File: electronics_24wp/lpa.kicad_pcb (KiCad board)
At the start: 2 copper layers, 143 x 74 mm, 89 parts, among them IC1 ATMEGA328-A, P1 CONN_2, P2 CONN_3X2, U1 SD_CARD, U2 LD1117S33, U3 TLC5941, U4 TLC5941, U5 TLC5941, Y1 RESONATEUR

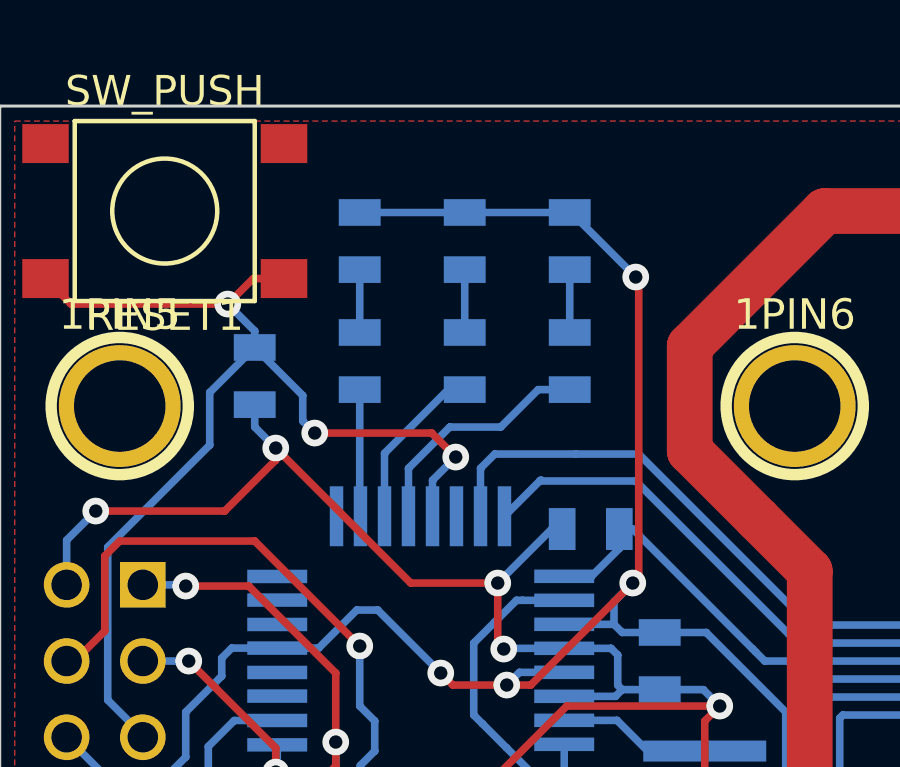
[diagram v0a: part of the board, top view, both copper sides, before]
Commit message: Changed the orientation of the leds in the electronic board.
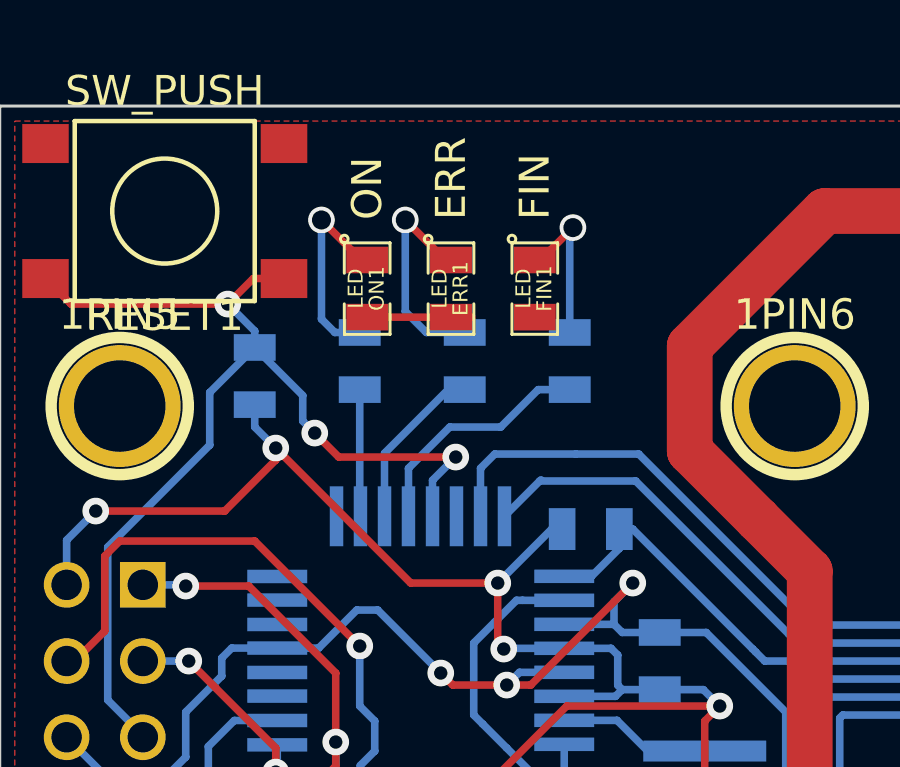
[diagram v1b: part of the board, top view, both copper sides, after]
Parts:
- ERR1, FIN1, ON1: moved to F.Cu
- moved FIN1 1.97 mm to (84.8, 100.6), turned to 270 degrees
- moved ERR1 1.65 mm to (82.0, 100.6), turned to 270 degrees
- moved ON1 1.60 mm to (79.2, 100.6), turned to 270 degrees
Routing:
- net GND: track 152.8 -> 136.1 mm, vias 7 -> 6
- net N-000005: track 2.09 -> 7.40 mm, vias 0 -> 1
- net N-000004: track 2.09 -> 6.84 mm, vias 0 -> 1
- net N-000006: track 2.09 -> 5.42 mm, vias 0 -> 1

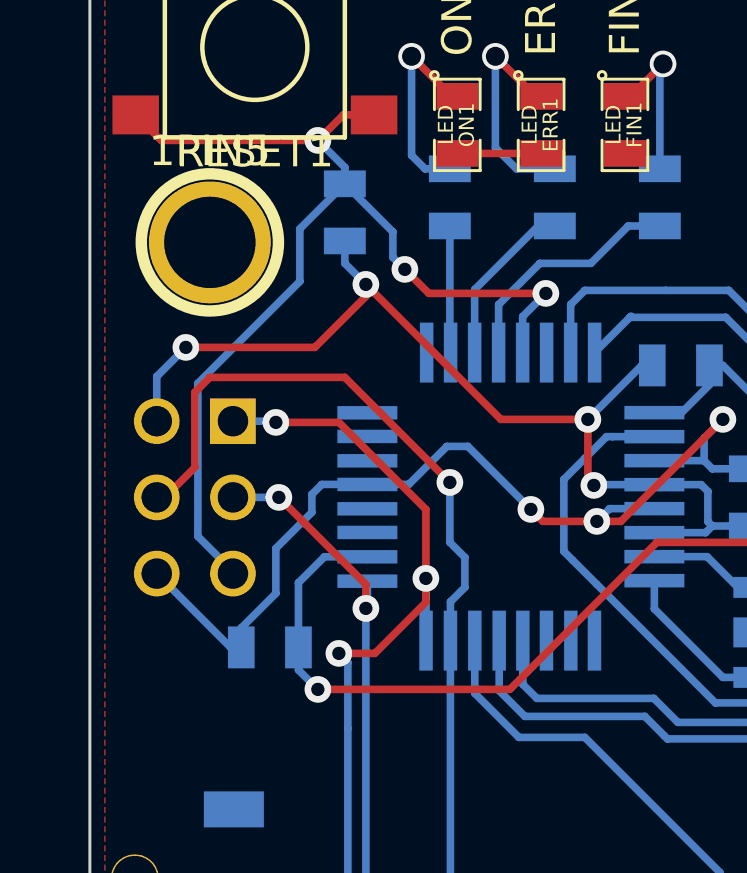
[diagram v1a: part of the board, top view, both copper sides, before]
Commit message: Changed the orientation of the programming connector.
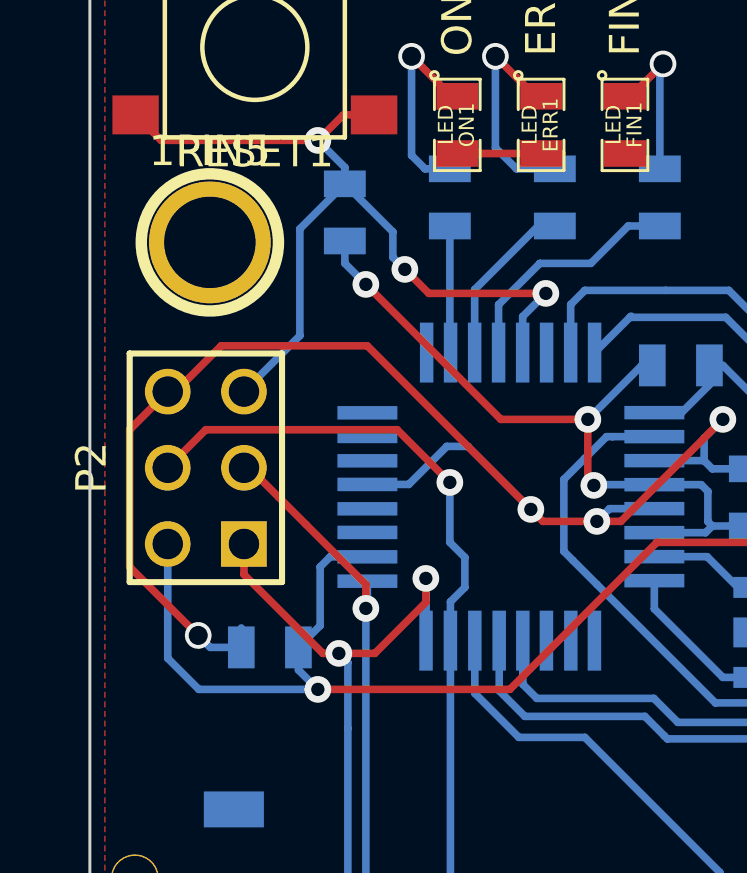
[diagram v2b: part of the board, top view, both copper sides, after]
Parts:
- P2: moved to F.Cu
- moved P2 1.05 mm to (70.9, 112.0), turned to 90 degrees
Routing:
- net GND: track 136.1 -> 151.4 mm, vias 6 -> 7
- net /RST: track 37.0 -> 29.8 mm
- net /MISO: track 57.4 -> 52.8 mm, vias 5 -> 4
- net /MOSI: track 51.9 -> 48.2 mm
- net /tlcs_1-3/VCC: track 309.7 -> 308.9 mm, vias 20 -> 19
- net /SCK: vias 4 -> 3

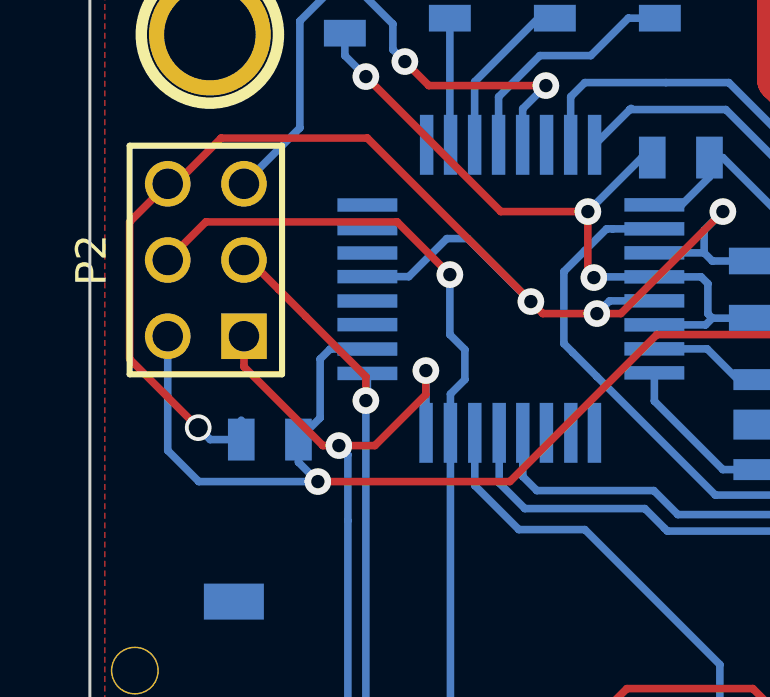
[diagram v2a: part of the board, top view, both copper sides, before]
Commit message: Added pin 1 indicator on programming connector.
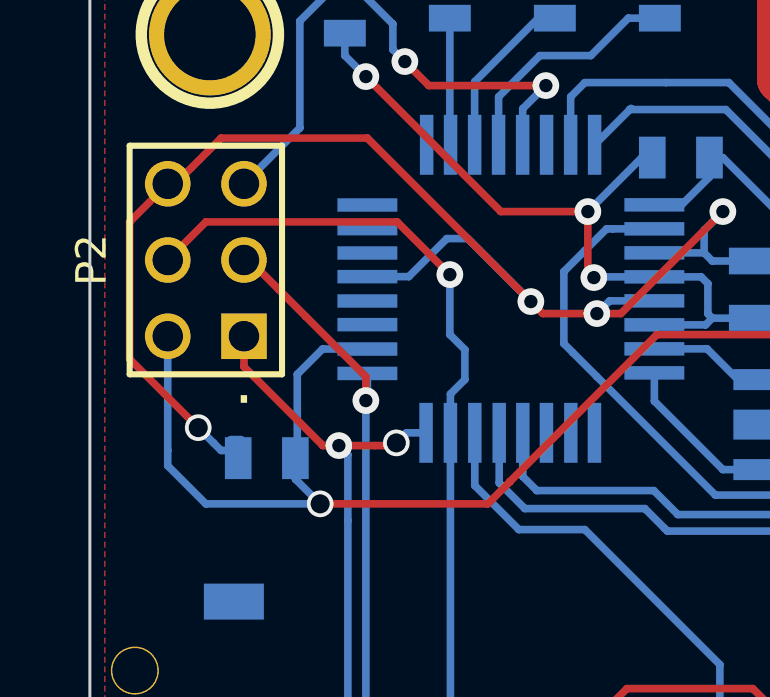
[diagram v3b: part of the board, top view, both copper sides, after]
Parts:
- moved C2 0.63 mm to (72.9, 118.6)
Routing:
- net /MISO: track 52.8 -> 49.4 mm
- net /tlcs_1-3/VCC: track 308.9 -> 310.8 mm
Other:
- board text added: "."
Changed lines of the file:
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@@
     (area 65.170999 88.399999 214.600001 176.600001)
     (thickness 1.6)
-    (drawings 59)
-    (tracks 1648)
+    (drawings 60)
+    (tracks 1652)
     (zones 0)
     (modules 89)
@@
   )
   (module SM0805 (layer B.Cu)
-    (at 73 118)
+    (at 72.898 118.618)
     (attr smd)
     (fp_text reference C2 (at 0 0.3175) (layer B.SilkS)
@@
     )
   )
+  (gr_text . (at 72.136 116.078) (layer F.SilkS)
+    (effects (font (size 1.5 1.5) (thickness 0.3)))
+  )
   (gr_line (start 214.5 88.5) (end 86.5 88.5) (angle 90) (layer Dwgs.User) (width 0.2))
   (gr_line (start 214.5 176.5) (end 214.5 88.5) (angle 90) (layer Dwgs.User) (width 0.2))
@@
   (segment (start 83.7 105.2) (end 82 105.2) (width 0.254) (layer B.Cu) (net 2))
   (segment (start 84.9475 103.9525) (end 83.7 105.2) (width 0.254) (layer B.Cu) (net 2))
+  (segment (start 78.206 117.7752) (end 77.5508 117.7752) (width 0.254) (layer B.Cu) (net 3))
+  (segment (start 76.5 118.2) (end 75.3 118.2) (width 0.254) (layer F.Cu) (net 3))
+  (segment (start 77.126 118.2) (end 76.5 118.2) (width 0.254) (layer F.Cu) (net 3))
+  (segment (start 77.216 118.11) (end 77.126 118.2) (width 0.254) (layer F.Cu) (net 3))
+  (via (at 77.216 118.11) (size 0.889) (drill 0.635) (layers F.Cu B.Cu) (net 3))
+  (segment (start 77.5508 117.7752) (end 77.216 118.11) (width 0.254) (layer B.Cu) (net 3))
   (segment (start 75.3 118.2) (end 74.766 118.2) (width 0.254) (layer F.Cu) (net 3))
   (segment (start 72.136 115.57) (end 72.136 114.554) (width 0.254) (layer F.Cu) (net 3))
@@
   (segment (start 75.6 137.9) (end 75.6 120.7) (width 0.254) (layer B.Cu) (net 3))
   (segment (start 78.2 140.5) (end 75.6 137.9) (width 0.254) (layer B.Cu) (net 3))
-  (segment (start 78.2 116.5) (end 78.2 115.7) (width 0.254) (layer F.Cu) (net 3))
-  (segment (start 76.5 118.2) (end 78.2 116.5) (width 0.254) (layer F.Cu) (net 3))
-  (segment (start 75.3 118.2) (end 76.5 118.2) (width 0.254) (layer F.Cu) (net 3))
   (via (at 75.3 118.2) (size 0.889) (layers F.Cu B.Cu) (net 3))
   (segment (start 75.6 118.5) (end 75.3 118.2) (width 0.254) (layer B.Cu) (net 3))
@@
   (via (at 90.5 145.5) (size 0.889) (layers F.Cu B.Cu) (net 3))
   (segment (start 90.83 145.83) (end 90.5 145.5) (width 0.254) (layer B.Cu) (net 3))
-  (segment (start 78.206 115.706) (end 78.206 117.7752) (width 0.254) (layer B.Cu) (net 3))
-  (via (at 78.2 115.7) (size 0.889) (layers F.Cu B.Cu) (net 3))
-  (segment (start 78.2 115.7) (end 78.206 115.706) (width 0.254) (layer B.Cu) (net 3))
   (segment (start 69.596 112.014) (end 70.866 110.744) (width 0.254) (layer F.Cu) (net 4))
   (segment (start 79.0188 116.4812) (end 79.0188 117.7752) (width 0.254) (layer B.Cu) (net 4))
@@
   (via (at 131.1 111.4) (size 0.889) (layers F.Cu B.Cu) (net 13))
   (segment (start 130.9 111.2) (end 131.1 111.4) (width 0.254) (layer B.Cu) (net 13))
-  (segment (start 76.2502 114.9812) (end 75.0108 114.9812) (width 0.254) (layer B.Cu) (net 14))
-  (segment (start 74.676 117.2765) (end 73.9525 118) (width 0.254) (layer B.Cu) (net 14))
-  (segment (start 74.676 115.316) (end 74.676 117.2765) (width 0.254) (layer B.Cu) (net 14))
-  (segment (start 75.0108 114.9812) (end 74.676 115.316) (width 0.254) (layer B.Cu) (net 14))
-  (segment (start 69.596 114.554) (end 69.596 118.364) (width 0.254) (layer B.Cu) (net 14))
-  (segment (start 70.632 119.4) (end 74.6 119.4) (width 0.254) (layer B.Cu) (net 14))
-  (segment (start 69.596 118.364) (end 70.632 119.4) (width 0.254) (layer B.Cu) (net 14))
+  (segment (start 74.676 120.142) (end 70.866 120.142) (width 0.254) (layer B.Cu) (net 14))
+  (segment (start 69.596 118.364) (end 69.596 114.554) (width 0.254) (layer B.Cu) (net 14))
+  (segment (start 69.596 118.364) (end 69.596 118.872) (width 0.254) (layer B.Cu) (net 14))
+  (segment (start 70.866 120.142) (end 69.596 118.872) (width 0.254) (layer B.Cu) (net 14))
+  (segment (start 73.8505 118.618) (end 73.8505 119.3165) (width 0.254) (layer B.Cu) (net 14))
+  (segment (start 73.8505 119.3165) (end 74.676 120.142) (width 0.254) (layer B.Cu) (net 14))
+  (segment (start 91 114.5) (end 85.9 114.5) (width 0.254) (layer F.Cu) (net 14))
+  (segment (start 85.9 114.5) (end 81 119.4) (width 0.254) (layer F.Cu) (net 14))
+  (segment (start 81 119.406) (end 81 119.4) (width 0.254) (layer F.Cu) (net 14))
+  (segment (start 80.264 120.142) (end 81 119.406) (width 0.254) (layer F.Cu) (net 14))
+  (segment (start 74.676 120.142) (end 80.264 120.142) (width 0.254) (layer F.Cu) (net 14))
+  (via (at 74.676 120.142) (size 0.889) (drill 0.635) (layers F.Cu B.Cu) (net 14))
+  (segment (start 74.7568 114.9812) (end 73.914 115.824) (width 0.254) (layer B.Cu) (net 14))
+  (segment (start 76.2502 114.9812) (end 74.7568 114.9812) (width 0.254) (layer B.Cu) (net 14))
+  (segment (start 73.914 115.824) (end 73.914 118.5545) (width 0.254) (layer B.Cu) (net 14))
+  (segment (start 73.914 118.5545) (end 73.8505 118.618) (width 0.254) (layer B.Cu) (net 14))
   (segment (start 170 126) (end 167.8 126) (width 0.254) (layer B.Cu) (net 14))
   (segment (start 181.8 127.5) (end 179.4 129.9) (width 0.254) (layer F.Cu) (net 14))
@@
   (segment (start 112.1 128.4475) (end 113.5475 127) (width 0.254) (layer B.Cu) (net 14))
   (segment (start 83.5475 133.5) (end 83.5475 131) (width 0.254) (layer F.Cu) (net 14))
-  (segment (start 91 114.5) (end 85.9 114.5) (width 0.254) (layer F.Cu) (net 14))
-  (segment (start 73.9525 118.7525) (end 73.9525 118) (width 0.254) (layer B.Cu) (net 14))
-  (segment (start 74.6 119.4) (end 73.9525 118.7525) (width 0.254) (layer B.Cu) (net 14))
-  (via (at 74.6 119.4) (size 0.889) (layers F.Cu B.Cu) (net 14))
-  (segment (start 81 119.4) (end 74.6 119.4) (width 0.254) (layer F.Cu) (net 14))
-  (segment (start 85.9 114.5) (end 81 119.4) (width 0.254) (layer F.Cu) (net 14))
   (segment (start 83.5475 128.5) (end 83.5475 127.6525) (width 0.254) (layer F.Cu) (net 14))
   (segment (start 89.1 126.3) (end 90.5 127.7) (width 0.254) (layer F.Cu) (net 14))
@@
   (segment (start 127.4 115.2) (end 127.4 116.9) (width 0.254) (layer B.Cu) (net 16))
   (segment (start 127 114.8) (end 127.4 115.2) (width 0.254) (layer B.Cu) (net 16))
-  (segment (start 72.0475 118) (end 71.01 118) (width 0.254) (layer B.Cu) (net 17))
-  (segment (start 68.326 110.744) (end 69.596 109.474) (width 0.254) (layer F.Cu) (net 17))
-  (segment (start 68.326 115.316) (end 68.326 110.744) (width 0.254) (layer F.Cu) (net 17))
-  (segment (start 70.612 117.602) (end 68.326 115.316) (width 0.254) (layer F.Cu) (net 17))
+  (segment (start 70.612 117.602) (end 71.12 118.11) (width 0.254) (layer B.Cu) (net 17))
   (via (at 70.612 117.602) (size 0.889) (drill 0.635) (layers F.Cu B.Cu) (net 17))
-  (segment (start 71.01 118) (end 70.612 117.602) (width 0.254) (layer B.Cu) (net 17))
+  (segment (start 70.612 117.602) (end 68.326 115.316) (width 0.254) (layer F.Cu) (net 17))
+  (segment (start 68.326 115.316) (end 68.326 110.744) (width 0.254) (layer F.Cu) (net 17))
+  (segment (start 69.596 109.474) (end 68.326 110.744) (width 0.254) (layer F.Cu) (net 17))
+  (segment (start 71.374 118.364) (end 71.6915 118.364) (width 0.254) (layer B.Cu) (net 17))
+  (segment (start 71.12 118.11) (end 71.374 118.364) (width 0.254) (layer B.Cu) (net 17))
+  (segment (start 71.6915 118.364) (end 71.9455 118.618) (width 0.254) (layer B.Cu) (net 17))
   (segment (start 69.596 109.474) (end 69.85 109.474) (width 0.254) (layer F.Cu) (net 17))
   (segment (start 69.85 109.474) (end 71.374 107.95) (width 0.254) (layer F.Cu) (net 17))
@@
   (segment (start 82.1 113.8) (end 83.9 113.8) (width 0.254) (layer F.Cu) (net 17))
   (segment (start 81.7 113.4) (end 82.1 113.8) (width 0.254) (layer F.Cu) (net 17))
-  (segment (start 72.0475 118) (end 72.0475 117.3525) (width 0.254) (layer B.Cu) (net 17))
   (segment (start 94.3 144.89) (end 94.3 138) (width 0.254) (layer B.Cu) (net 17))
   (segment (start 93.1 136.8) (end 92.81 136.8) (width 0.254) (layer B.Cu) (net 17) (status 30))

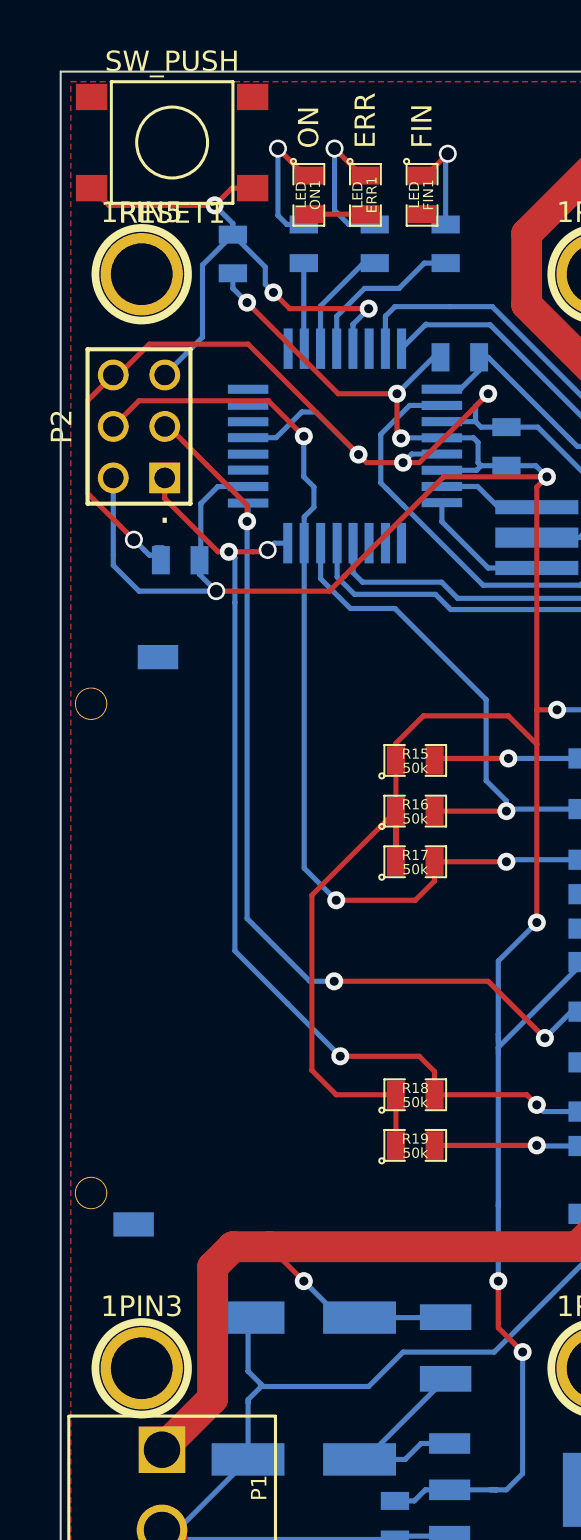
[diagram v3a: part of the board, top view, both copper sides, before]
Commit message: Moved status LEDs to fit with the 3d-printed parts.
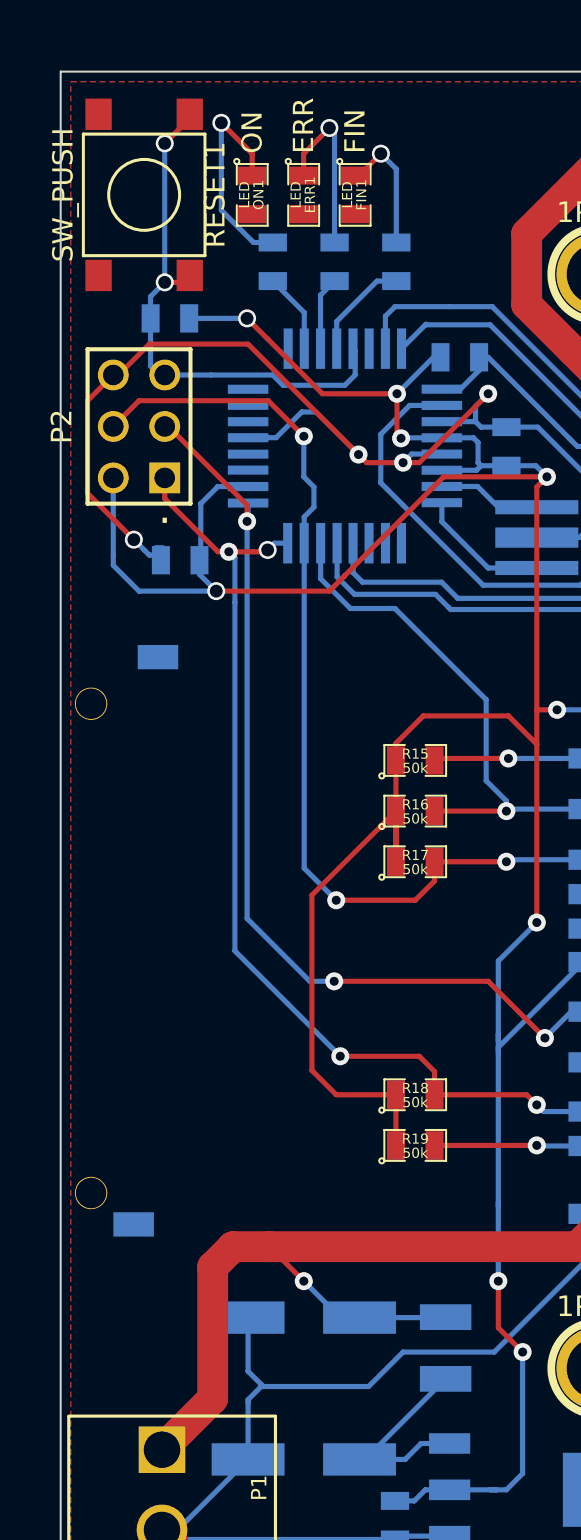
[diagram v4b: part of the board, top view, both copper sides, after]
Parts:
- removed 1PIN3, 1PIN5: P***, 1pin
- moved R1 4.45 mm to (72.4, 106.7), turned to 0 degrees
- moved FIN1 3.30 mm to (81.5, 100.6)
- moved ERR1 3.05 mm to (79.0, 100.6)
- moved RESET1 2.93 mm to (71.1, 100.6), turned to 270 degrees
- moved ON1 2.79 mm to (76.5, 100.6)
- moved R_FIN1 2.59 mm to (83.6, 103.9)
- moved R_ERR1 2.17 mm to (80.5, 103.9)
- moved R_ON1 1.77 mm to (77.5, 103.9)
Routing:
- net N-000004: track 6.84 -> 10.8 mm
- net GND: track 150.9 -> 147.2 mm
- net /RST: track 29.8 -> 26.6 mm, vias 3 -> 2
- net /FIN: track 8.06 -> 5.11 mm
- net /ERR: track 5.65 -> 3.62 mm
- net N-000005: track 7.40 -> 8.63 mm
- net N-000006: track 5.42 -> 6.48 mm
- net /tlcs_1-3/VCC: track 310.8 -> 311.6 mm
